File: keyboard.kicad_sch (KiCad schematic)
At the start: 120 parts, among them SW1 SW_Push, SW10 SW_Push, SW11 SW_Push, SW12 SW_Push, SW13 SW_Push, SW14 SW_Push, SW15 SW_Push, SW16 SW_Push, SW17 SW_Push, SW18 SW_Push, SW19 SW_Push, SW2 SW_Push, SW20 SW_Push, SW21 SW_Push, SW22 SW_Push, SW23 SW_Push, SW24 SW_Push, SW25 SW_Push, SW26 SW_Push, SW27 SW_Push, SW28 SW_Push, SW29 SW_Push, SW3 SW_Push, SW30 SW_Push, SW31 SW_Push, SW32 SW_Push, SW33 SW_Push, SW34 SW_Push, SW35 SW_Push, SW36 SW_Push, SW37 SW_Push, SW38 SW_Push, SW39 SW_Push, SW4 SW_Push, SW40 SW_Push, SW41 SW_Push, SW42 SW_Push, SW43 SW_Push, SW44 SW_Push, SW45 SW_Push, SW46 SW_Push, SW47 SW_Push, SW48 SW_Push, SW49 SW_Push, SW5 SW_Push, SW50 SW_Push, SW51 SW_Push, SW52 SW_Push, SW53 SW_Push, SW54 SW_Push, SW55 SW_Push, SW56 SW_Push, SW57 SW_Push, SW58 SW_Push, SW59 SW_Push, SW6 SW_Push, SW60 SW_Push, SW7 SW_Push, SW8 SW_Push, SW9 SW_Push

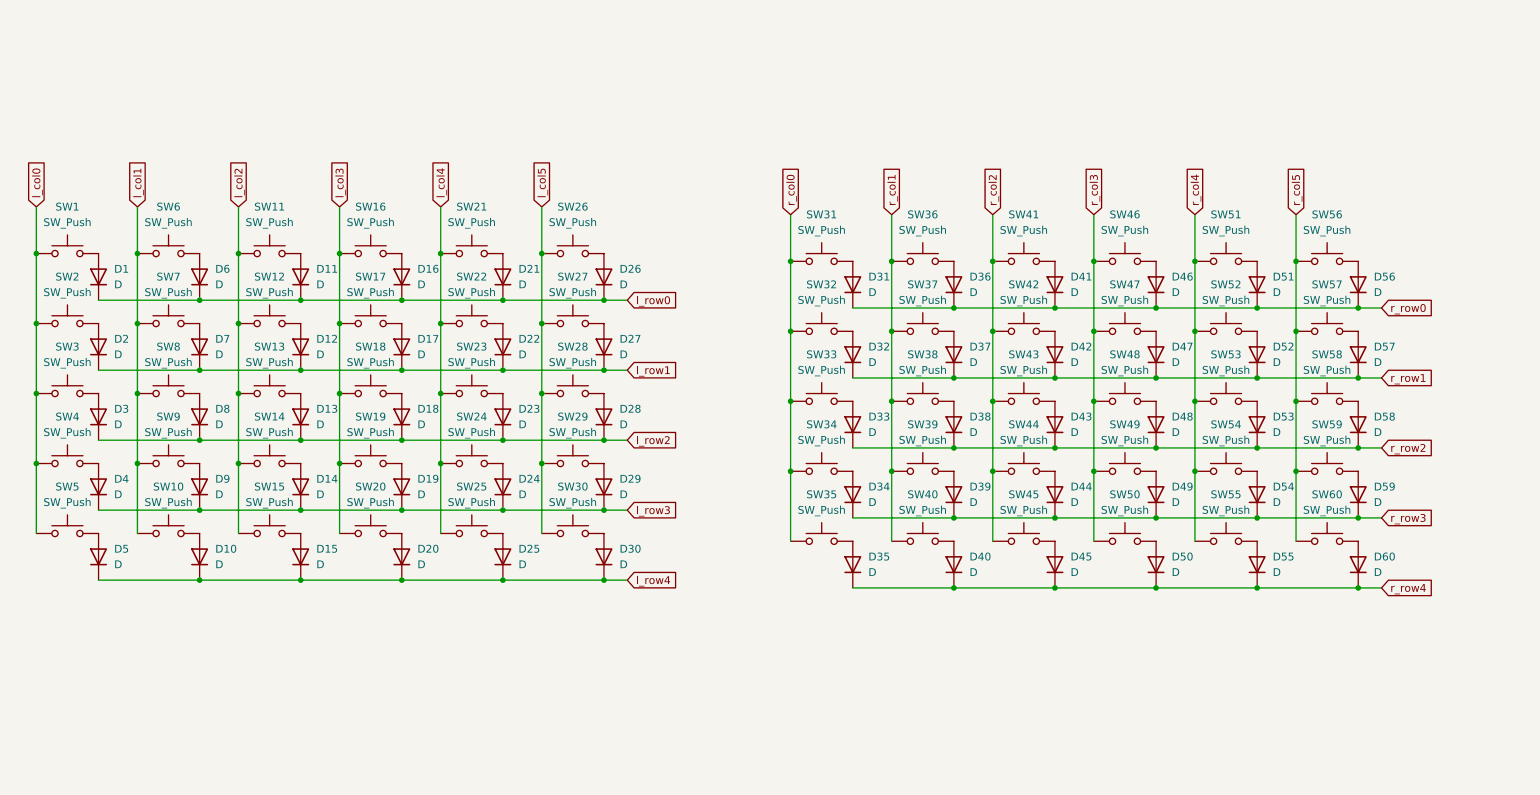
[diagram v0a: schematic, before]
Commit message: Add Waveshare-RP2040 board and TRS jack
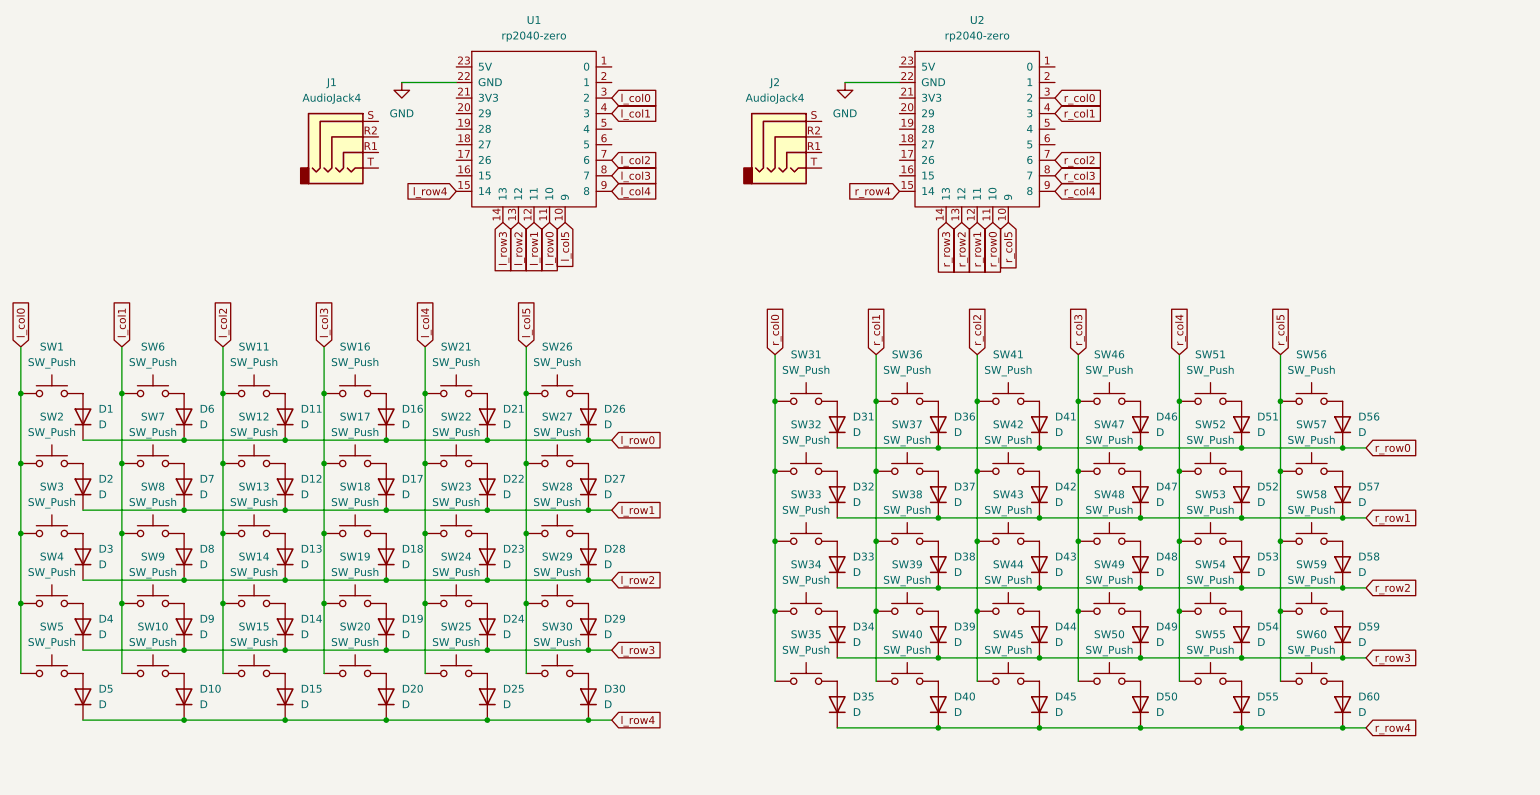
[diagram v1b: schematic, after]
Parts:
- added J1, J2: AudioJack4, symbol Connector_Audio:AudioJack4
- added U1, U2: rp2040-zero, symbol mcu:rp2040-zero
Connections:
- net l_col0: now also U1.3 (2)
- net l_col1: now also U1.4 (3)
- net l_col2: now also U1.7 (6)
- net l_col3: now also U1.8 (7)
- net l_col4: now also U1.9 (8)
- net l_col5: now also U1.10 (9)
- net l_row0: now also U1.11 (10)
- net l_row1: now also U1.12 (11)
- net l_row2: now also U1.13 (12)
- net l_row3: now also U1.14 (13)
- net l_row4: now also U1.15 (14)
- net r_col0: now also U2.3 (2)
- net r_col1: now also U2.4 (3)
- net r_col2: now also U2.7 (6)
- net r_col3: now also U2.8 (7)
- net r_col4: now also U2.9 (8)
- net r_col5: now also U2.10 (9)
- net r_row0: now also U2.11 (10)
- net r_row1: now also U2.12 (11)
- net r_row2: now also U2.13 (12)
- net r_row3: now also U2.14 (13)
- net r_row4: now also U2.15 (14)
- new net GND: U1.22 (GND), U2.22 (GND)
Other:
- moved on the sheet: D1, D10, D11, D12, D13, D14, D15, D16, D17, D18, D19, D2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

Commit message: Place all symbols on the schematic diagram
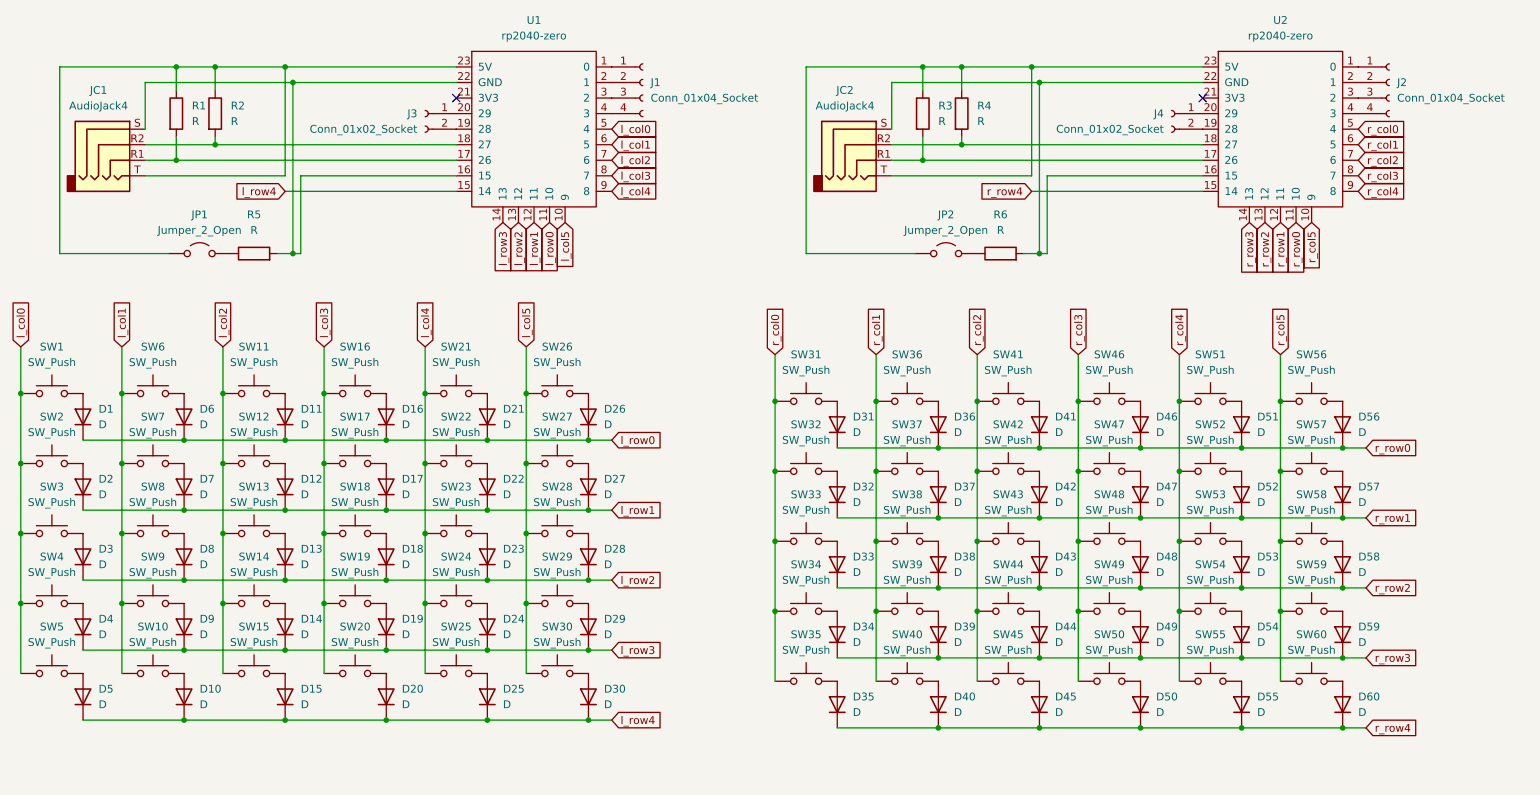
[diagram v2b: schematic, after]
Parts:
- added J1, J2: Conn_01x04_Socket, symbol Connector:Conn_01x04_Socket
- added J3, J4: Conn_01x02_Socket, symbol Connector:Conn_01x02_Socket
- added JP1, JP2: Jumper_2_Open, symbol Jumper:Jumper_2_Open
- added R1, R2, R3, R4, R5, R6: R, symbol Device:R
- renumbered J1 to JC1, J2 to JC2
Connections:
- net l_col0: now also U1.5 (4); no longer U1.3 (2)
- net l_col1: now also U1.6 (5); no longer U1.4 (3)
- net r_col0: now also U2.5 (4); no longer U2.3 (2)
- net r_col1: now also U2.6 (5); no longer U2.4 (3)
- net at U1.1 (0): now also J1.1 (Pin_1)
- net at U1.16 (15): now also JC1.S, U1.22 (GND), R5.2
- net at U1.17 (26): now also JC1.R1, R1.2
- net at U1.18 (27): now also JC1.R2, R2.2
- net at U1.19 (28): now also J3.2 (Pin_2)
- net at U1.2 (1): now also J1.2 (Pin_2)
- net at U1.20 (29): now also J3.1 (Pin_1)
- net at U1.23 (5V): now also JC1.T, JP1.1 (A), R1.1, R2.1
- net at U2.1 (0): now also J2.1 (Pin_1)
- net at U2.16 (15): now also JC2.S, U2.22 (GND), R6.2
- net at U2.17 (26): now also JC2.R1, R3.2
- net at U2.18 (27): now also JC2.R2, R4.2
- net at U2.19 (28): now also J4.2 (Pin_2)
- net at U2.2 (1): now also J2.2 (Pin_2)
- net at U2.20 (29): now also J4.1 (Pin_1)
- net at U2.23 (5V): now also JC2.T, JP2.1 (A), R3.1, R4.1
- removed net GND: U1.22 (GND), U2.22 (GND)
- new net: J1.3 (Pin_3), U1.3 (2)
- new net: J1.4 (Pin_4), U1.4 (3)
- new net: JP1.2 (B), R5.1
- new net: J2.3 (Pin_3), U2.3 (2)
- new net: J2.4 (Pin_4), U2.4 (3)
- new net: JP2.2 (B), R6.1
- no-connect marks 0 -> 2
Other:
- moved on the sheet: JC1, JC2, U2

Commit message: Once got the schematic down to just one side.
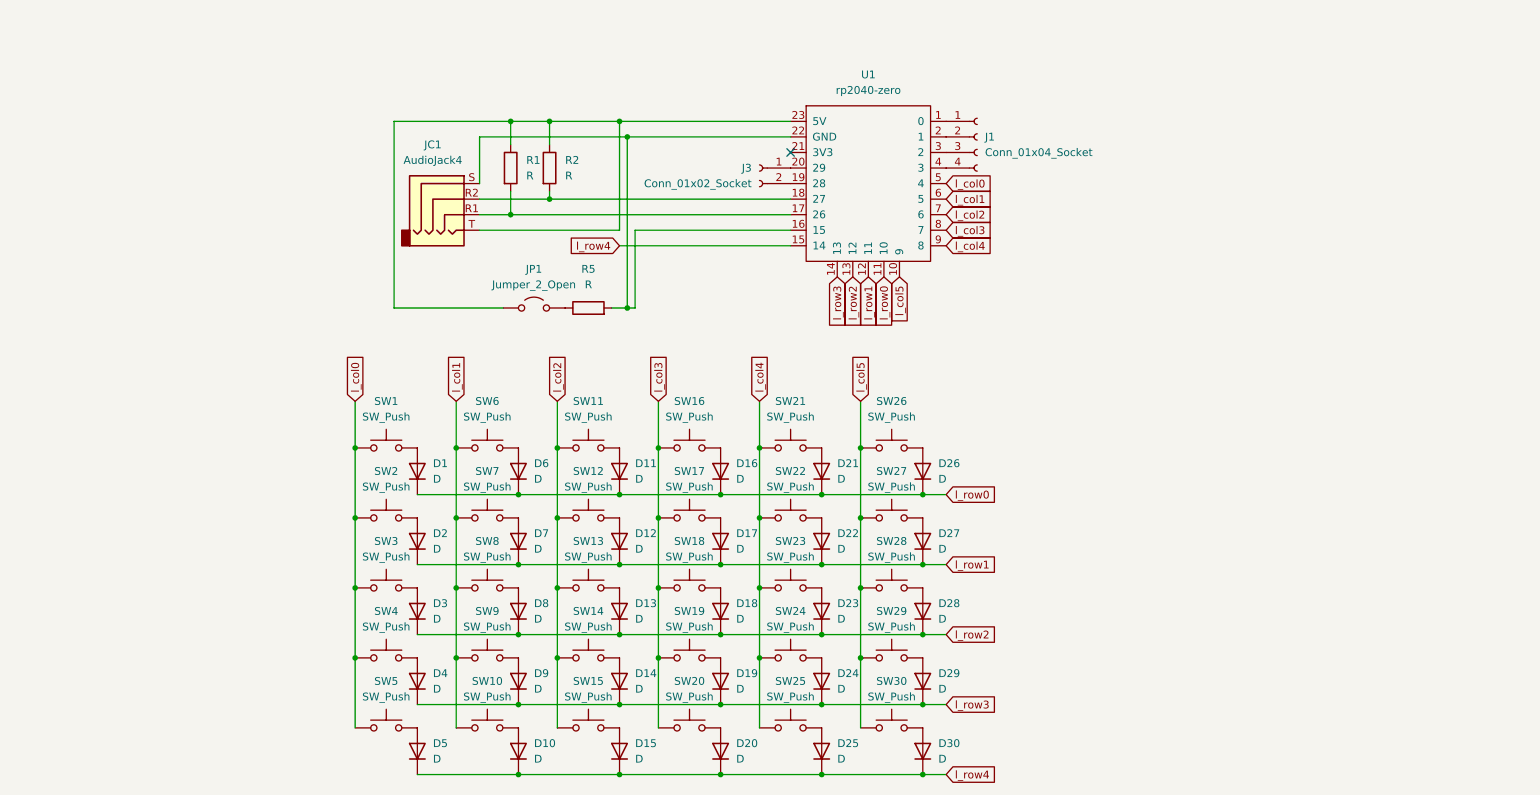
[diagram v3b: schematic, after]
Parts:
- removed D31, D32, D33, D34, D35, D36, D37, D38, D39, D40, D41, D42, D43, D44, D45, D46, D47, D48, D49, D50, D51, D52, D53, D54, D55, D56, D57, D58, D59, D60: D, symbol Device:D
- removed J2: Conn_01x04_Socket, symbol Connector:Conn_01x04_Socket
- removed J4: Conn_01x02_Socket, symbol Connector:Conn_01x02_Socket
- removed JC2: AudioJack4, symbol Connector_Audio:AudioJack4
- removed JP2: Jumper_2_Open, symbol Jumper:Jumper_2_Open
- removed R3, R4, R6: R, symbol Device:R
- removed SW31, SW32, SW33, SW34, SW35, SW36, SW37, SW38, SW39, SW40, SW41, SW42, SW43, SW44, SW45, SW46, SW47, SW48, SW49, SW50, SW51, SW52, SW53, SW54, SW55, SW56, SW57, SW58, SW59, SW60: SW_Push, symbol Switch:SW_Push
- removed U2: rp2040-zero, symbol mcu:rp2040-zero
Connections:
- no-connect marks 2 -> 1
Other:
- moved on the sheet: D1, D10, D11, D12, D13, D14, D15, D16, D17, D18, D19, D2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

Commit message: Apply footprints to each symbol
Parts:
- D1, D10, D11, D12, D13, D14, D15, D16, D17, D18, D19, D2, D20, D21, D22, D23, D24, D25, D26, D27, D28, D29, D3, D30, D4, D5, D6, D7, D8, D9: footprint (none) -> Diode_SMD:D_1210_3225Metric_Pad1.42x2.65mm_HandSolder
- J1: footprint (none) -> Connector_PinHeader_2.54mm:PinHeader_1x04_P2.54mm_Vertical
- J3: footprint (none) -> Connector_PinHeader_2.54mm:PinHeader_1x02_P2.54mm_Vertical
- JC1: footprint (none) -> Connector_Audio:Jack_3.5mm_PJ320E_Horizontal
- JP1: footprint (none) -> Jumper:SolderJumper-2_P1.3mm_Open_Pad1.0x1.5mm
- R1, R2, R5: footprint (none) -> Resistor_SMD:R_1210_3225Metric_Pad1.30x2.65mm_HandSolder
- SW1, SW10, SW11, SW12, SW13, SW14, SW15, SW16, SW17, SW18, SW19, SW2, SW20, SW21, SW22, SW23, SW24, SW25, SW26, SW27, SW28, SW29, SW3, SW30, SW4, SW5, SW6, SW7, SW8, SW9: footprint (none) -> kbd:keyswitch_cherrymx_hotswap_1u
- U1: footprint (none) -> mcu:rp2040-zero-tht

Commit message: 回路図のアノテーションを変更
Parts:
- renumbered D11 to D10, D12 to D11, D13 to D12, D14 to D13, D15 to D14, D16 to D15, D17 to D16, D18 to D17, D19 to D18, D21 to D19, D22 to D20, D23 to D21, D24 to D22, D25 to D23, D26 to D24, D27 to D25, D28 to D26, D29 to D27, D30 to D28, D5 to D401, D20 to D402, D6 to D5, D7 to D6, D8 to D7, D9 to D8, D10 to D9, SW11 to SW10, SW12 to SW11, SW13 to SW12, SW14 to SW13, SW15 to SW14, SW16 to SW15, SW17 to SW16, SW18 to SW17, SW19 to SW18, SW21 to SW19, SW22 to SW20, SW23 to SW21, SW24 to SW22, SW25 to SW23, SW26 to SW24, SW27 to SW25, SW28 to SW26, SW29 to SW27, SW30 to SW28, SW5 to SW401, SW20 to SW402, SW6 to SW5, SW7 to SW6, SW8 to SW7, SW9 to SW8, SW10 to SW9

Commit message: 部品のフットプリントを再設定
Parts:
- D1, D10, D11, D12, D13, D14, D15, D16, D17, D18, D19, D2, D20, D21, D22, D23, D24, D25, D26, D27, D28, D3, D4, D401, D402, D5, D6, D7, D8, D9: footprint Diode_SMD:D_1210_3225Metric_Pad1.42x2.65mm_HandSolder -> Diode_SMD:D_1206_3216Metric_Pad1.42x1.75mm_HandSolder
- R1, R2, R5: footprint Resistor_SMD:R_1210_3225Metric_Pad1.30x2.65mm_HandSolder -> Resistor_SMD:R_1206_3216Metric_Pad1.30x1.75mm_HandSolder
- SW401: footprint kbd:keyswitch_cherrymx_hotswap_1u -> Button_Switch_Keyboard:SW_Cherry_MX_2.00u_Plate
- SW402: footprint kbd:keyswitch_cherrymx_hotswap_1u -> Button_Switch_Keyboard:SW_Cherry_MX_2.00u_Vertical_Plate
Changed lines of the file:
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@@
 			)
 		)
-		(property "Footprint" "Diode_SMD:D_1210_3225Metric_Pad1.42x2.65mm_HandSolder"
+		(property "Footprint" "Diode_SMD:D_1206_3216Metric_Pad1.42x1.75mm_HandSolder"
 			(at 148.59 134.62 0)
 			(effects
@@
 			)
 		)
-		(property "Footprint" "Diode_SMD:D_1210_3225Metric_Pad1.42x2.65mm_HandSolder"
+		(property "Footprint" "Diode_SMD:D_1206_3216Metric_Pad1.42x1.75mm_HandSolder"
 			(at 181.61 111.76 0)
 			(effects
@@
 			)
 		)
-		(property "Footprint" "Diode_SMD:D_1210_3225Metric_Pad1.42x2.65mm_HandSolder"
+		(property "Footprint" "Diode_SMD:D_1206_3216Metric_Pad1.42x1.75mm_HandSolder"
 			(at 132.08 146.05 0)
 			(effects
@@
 			)
 		)
-		(property "Footprint" "Diode_SMD:D_1210_3225Metric_Pad1.42x2.65mm_HandSolder"
+		(property "Footprint" "Diode_SMD:D_1206_3216Metric_Pad1.42x1.75mm_HandSolder"
 			(at 115.57 100.33 0)
 			(effects
@@
 			)
 		)
-		(property "Footprint" "Diode_SMD:D_1210_3225Metric_Pad1.42x2.65mm_HandSolder"
+		(property "Footprint" "Diode_SMD:D_1206_3216Metric_Pad1.42x1.75mm_HandSolder"
 			(at 165.1 134.62 0)
 			(effects
@@
 			)
 		)
-		(property "Footprint" "Diode_SMD:D_1210_3225Metric_Pad1.42x2.65mm_HandSolder"
+		(property "Footprint" "Diode_SMD:D_1206_3216Metric_Pad1.42x1.75mm_HandSolder"
 			(at 181.61 134.62 0)
 			(effects
@@
 			)
 		)
-		(property "Footprint" "Diode_SMD:D_1210_3225Metric_Pad1.42x2.65mm_HandSolder"
+		(property "Footprint" "Diode_SMD:D_1206_3216Metric_Pad1.42x1.75mm_HandSolder"
 			(at 99.06 134.62 0)
 			(effects
@@
 			)
 		)
-		(property "Footprint" "Diode_SMD:D_1210_3225Metric_Pad1.42x2.65mm_HandSolder"
+		(property "Footprint" "Diode_SMD:D_1206_3216Metric_Pad1.42x1.75mm_HandSolder"
 			(at 132.08 111.76 0)
 			(effects
@@
 			)
 		)
-		(property "Footprint" "Diode_SMD:D_1210_3225Metric_Pad1.42x2.65mm_HandSolder"
+		(property "Footprint" "Diode_SMD:D_1206_3216Metric_Pad1.42x1.75mm_HandSolder"
 			(at 148.59 123.19 0)
 			(effects
@@
 			)
 		)
-		(property "Footprint" "Diode_SMD:D_1210_3225Metric_Pad1.42x2.65mm_HandSolder"
+		(property "Footprint" "Diode_SMD:D_1206_3216Metric_Pad1.42x1.75mm_HandSolder"
 			(at 165.1 146.05 0)
 			(effects
@@
 			)
 		)
-		(property "Footprint" "Diode_SMD:D_1210_3225Metric_Pad1.42x2.65mm_HandSolder"
+		(property "Footprint" "Diode_SMD:D_1206_3216Metric_Pad1.42x1.75mm_HandSolder"
 			(at 165.1 111.76 0)
 			(effects
@@
 			)
 		)
-		(property "Footprint" "Diode_SMD:D_1210_3225Metric_Pad1.42x2.65mm_HandSolder"
+		(property "Footprint" "Diode_SMD:D_1206_3216Metric_Pad1.42x1.75mm_HandSolder"
 			(at 148.59 100.33 0)
 			(effects
@@
 			)
 		)
-		(property "Footprint" "kbd:keyswitch_cherrymx_hotswap_1u"
+		(property "Footprint" "Button_Switch_Keyboard:SW_Cherry_MX_2.00u_Vertical_Plate"
 			(at 143.51 137.16 0)
 			(effects
@@
 			)
 		)
-		(property "Footprint" "Diode_SMD:D_1210_3225Metric_Pad1.42x2.65mm_HandSolder"
+		(property "Footprint" "Diode_SMD:D_1206_3216Metric_Pad1.42x1.75mm_HandSolder"
 			(at 132.08 134.62 0)
 			(effects
@@
 			)
 		)
-		(property "Footprint" "Diode_SMD:D_1210_3225Metric_Pad1.42x2.65mm_HandSolder"
+		(property "Footprint" "Diode_SMD:D_1206_3216Metric_Pad1.42x1.75mm_HandSolder"
 			(at 181.61 123.19 0)
 			(effects
@@
 			)
 		)
-		(property "Footprint" "Resistor_SMD:R_1210_3225Metric_Pad1.30x2.65mm_HandSolder"
+		(property "Footprint" "Resistor_SMD:R_1206_3216Metric_Pad1.30x1.75mm_HandSolder"
 			(at 127 75.438 90)
 			(effects
@@
 			)
 		)
-		(property "Footprint" "Diode_SMD:D_1210_3225Metric_Pad1.42x2.65mm_HandSolder"
+		(property "Footprint" "Diode_SMD:D_1206_3216Metric_Pad1.42x1.75mm_HandSolder"
 			(at 148.59 111.76 0)
 			(effects
@@
 			)
 		)
-		(property "Footprint" "Diode_SMD:D_1210_3225Metric_Pad1.42x2.65mm_HandSolder"
+		(property "Footprint" "Diode_SMD:D_1206_3216Metric_Pad1.42x1.75mm_HandSolder"
 			(at 115.57 111.76 0)
 			(effects
@@
 			)
 		)
-		(property "Footprint" "Diode_SMD:D_1210_3225Metric_Pad1.42x2.65mm_HandSolder"
+		(property "Footprint" "Diode_SMD:D_1206_3216Metric_Pad1.42x1.75mm_HandSolder"
 			(at 99.06 123.19 0)
 			(effects
@@
 			)
 		)
-		(property "Footprint" "Diode_SMD:D_1210_3225Metric_Pad1.42x2.65mm_HandSolder"
+		(property "Footprint" "Diode_SMD:D_1206_3216Metric_Pad1.42x1.75mm_HandSolder"
 			(at 99.06 146.05 0)
 			(effects
@@
 			)
 		)
-		(property "Footprint" "Diode_SMD:D_1210_3225Metric_Pad1.42x2.65mm_HandSolder"
+		(property "Footprint" "Diode_SMD:D_1206_3216Metric_Pad1.42x1.75mm_HandSolder"
 			(at 115.57 146.05 0)
 			(effects
@@
 			)
 		)
-		(property "Footprint" "Diode_SMD:D_1210_3225Metric_Pad1.42x2.65mm_HandSolder"
+		(property "Footprint" "Diode_SMD:D_1206_3216Metric_Pad1.42x1.75mm_HandSolder"
 			(at 115.57 134.62 0)
 			(effects
@@
 			)
 		)
-		(property "Footprint" "Diode_SMD:D_1210_3225Metric_Pad1.42x2.65mm_HandSolder"
+		(property "Footprint" "Diode_SMD:D_1206_3216Metric_Pad1.42x1.75mm_HandSolder"
 			(at 181.61 100.33 0)
 			(effects
@@
 			)
 		)
-		(property "Footprint" "Diode_SMD:D_1210_3225Metric_Pad1.42x2.65mm_HandSolder"
+		(property "Footprint" "Diode_SMD:D_1206_3216Metric_Pad1.42x1.75mm_HandSolder"
 			(at 181.61 146.05 0)
 			(effects
@@
 			)
 		)
-		(property "Footprint" "Diode_SMD:D_1210_3225Metric_Pad1.42x2.65mm_HandSolder"
+		(property "Footprint" "Diode_SMD:D_1206_3216Metric_Pad1.42x1.75mm_HandSolder"
 			(at 148.59 146.05 0)
 			(effects
@@
 			)
 		)
-		(property "Footprint" "Resistor_SMD:R_1210_3225Metric_Pad1.30x2.65mm_HandSolder"
+		(property "Footprint" "Resistor_SMD:R_1206_3216Metric_Pad1.30x1.75mm_HandSolder"
 			(at 118.872 50.8 90)
 			(effects
@@
 			)
 		)
-		(property "Footprint" "Resistor_SMD:R_1210_3225Metric_Pad1.30x2.65mm_HandSolder"
+		(property "Footprint" "Resistor_SMD:R_1206_3216Metric_Pad1.30x1.75mm_HandSolder"
 			(at 112.522 50.8 90)
 			(effects
@@
 			)
 		)
-		(property "Footprint" "Diode_SMD:D_1210_3225Metric_Pad1.42x2.65mm_HandSolder"
+		(property "Footprint" "Diode_SMD:D_1206_3216Metric_Pad1.42x1.75mm_HandSolder"
 			(at 132.08 100.33 0)
 			(effects
@@
 			)
 		)
-		(property "Footprint" "Diode_SMD:D_1210_3225Metric_Pad1.42x2.65mm_HandSolder"
+		(property "Footprint" "Diode_SMD:D_1206_3216Metric_Pad1.42x1.75mm_HandSolder"
 			(at 132.08 123.19 0)
 			(effects
@@
 			)
 		)
-		(property "Footprint" "kbd:keyswitch_cherrymx_hotswap_1u"
+		(property "Footprint" "Button_Switch_Keyboard:SW_Cherry_MX_2.00u_Plate"
 			(at 93.98 137.16 0)
 			(effects
@@
 			)
 		)
-		(property "Footprint" "Diode_SMD:D_1210_3225Metric_Pad1.42x2.65mm_HandSolder"
+		(property "Footprint" "Diode_SMD:D_1206_3216Metric_Pad1.42x1.75mm_HandSolder"
 			(at 115.57 123.19 0)
 			(effects
@@
 			)
 		)
-		(property "Footprint" "Diode_SMD:D_1210_3225Metric_Pad1.42x2.65mm_HandSolder"
+		(property "Footprint" "Diode_SMD:D_1206_3216Metric_Pad1.42x1.75mm_HandSolder"
 			(at 165.1 100.33 0)
 			(effects
@@
 			)
 		)
-		(property "Footprint" "Diode_SMD:D_1210_3225Metric_Pad1.42x2.65mm_HandSolder"
+		(property "Footprint" "Diode_SMD:D_1206_3216Metric_Pad1.42x1.75mm_HandSolder"
 			(at 165.1 123.19 0)
 			(effects
@@
 			)
 		)
-		(property "Footprint" "Diode_SMD:D_1210_3225Metric_Pad1.42x2.65mm_HandSolder"
+		(property "Footprint" "Diode_SMD:D_1206_3216Metric_Pad1.42x1.75mm_HandSolder"
 			(at 99.06 100.33 0)
 			(effects
@@
 			)
 		)
-		(property "Footprint" "Diode_SMD:D_1210_3225Metric_Pad1.42x2.65mm_HandSolder"
+		(property "Footprint" "Diode_SMD:D_1206_3216Metric_Pad1.42x1.75mm_HandSolder"
 			(at 99.06 111.76 0)
 			(effects
